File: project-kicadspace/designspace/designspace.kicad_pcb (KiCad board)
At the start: 2 copper layers, 39 parts, among them J1 PJ-313B, U3 MAX9812

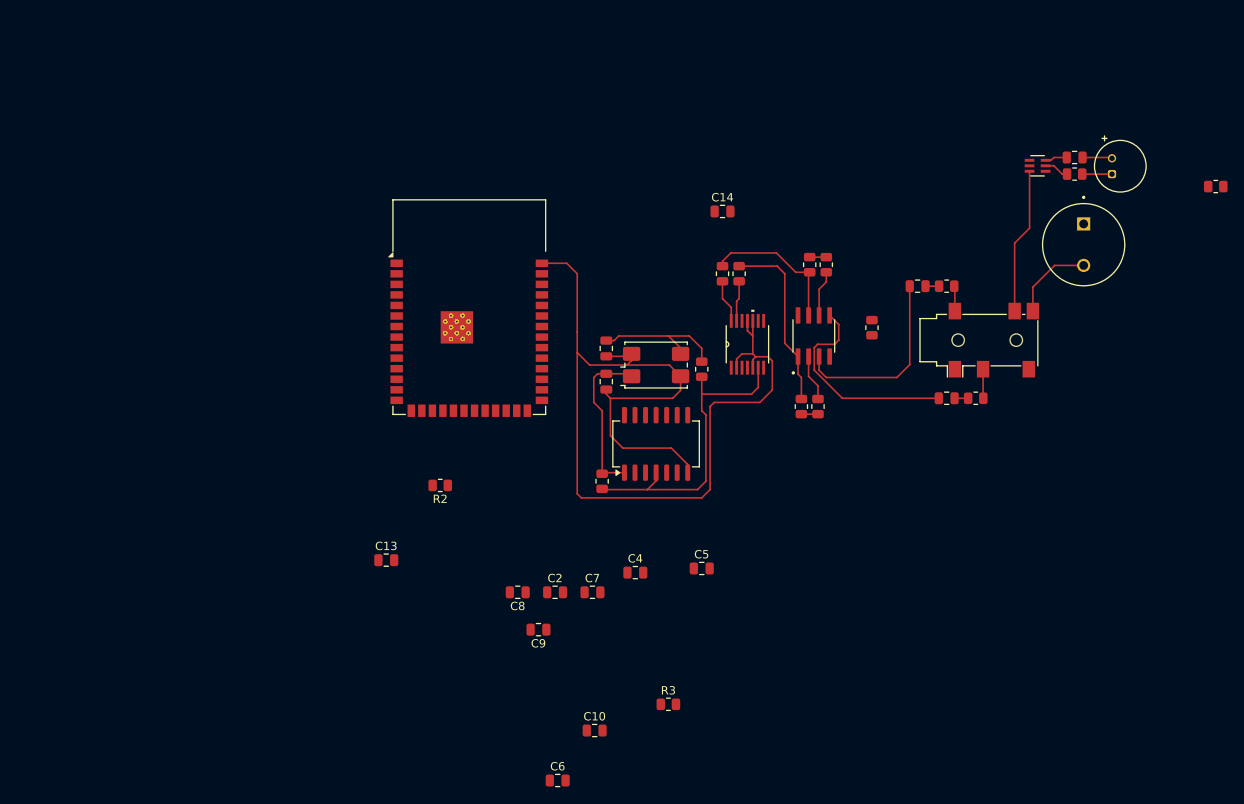
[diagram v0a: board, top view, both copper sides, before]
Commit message: feat(pcb): add kit footprint for esp32 & inital placing
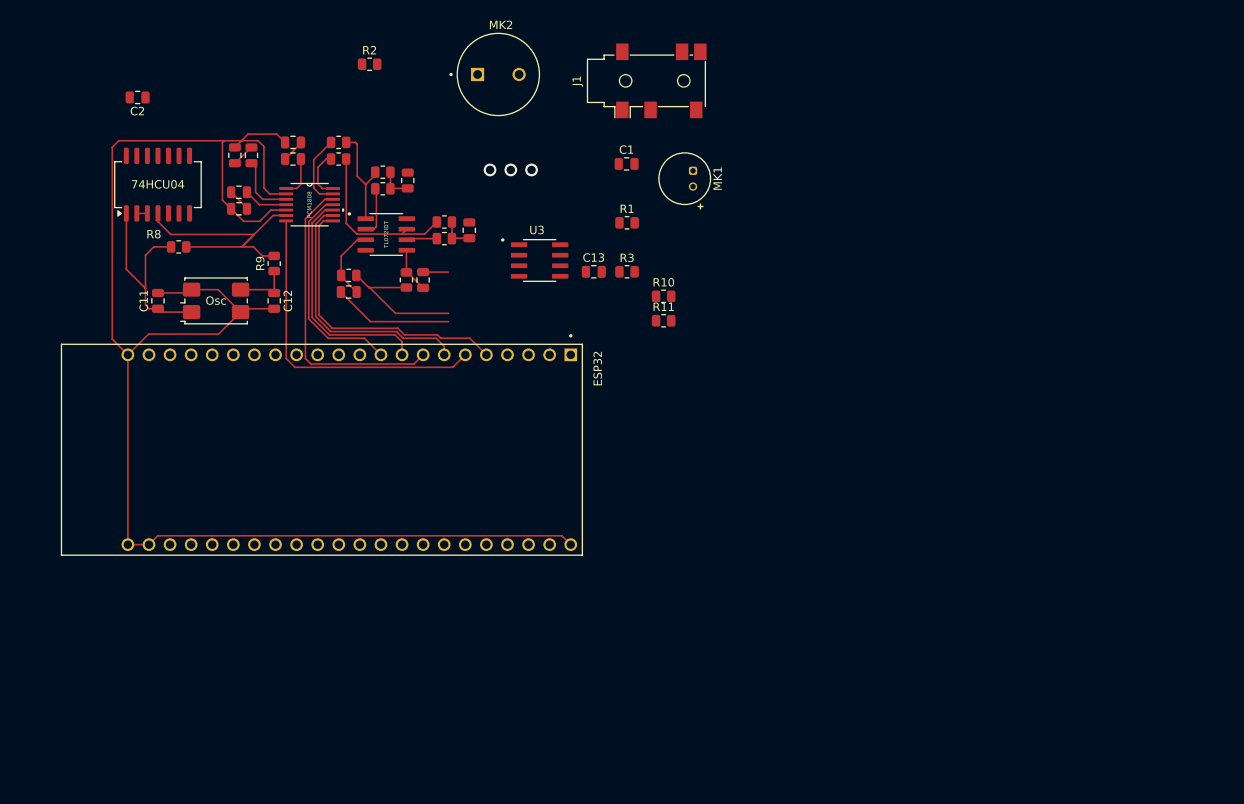
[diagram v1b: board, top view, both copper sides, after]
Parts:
- removed INVBUF1: 74HCU04, Package_SO:SO-14_5.3x10.2mm_P1.27mm
- removed Op-amp2: TL072, tl072:TL072IDT
- removed Osc1: 24.576MHz, Crystal:Crystal_SMD_7050-4Pin_7.0x5.0mm
- added 74HCU04: 74HCU04, Package_SO:SO-14_5.3x10.2mm_P1.27mm, F.Cu at (59.0, 70.3)
- added Osc: 24.576MHz, Crystal:Crystal_SMD_7050-4Pin_7.0x5.0mm, F.Cu at (66.0, 84.3)
- added TL072IDT: TL072, tl072:TL072IDT, F.Cu at (86.5, 76.3)
- ESP32: value ESP32-S3-WROOM-1 -> ESP32-S3-DEVKITC-1-N8R8; footprint RF_Module:ESP32-S3-WROOM-1 -> esp32-s3-kit:ESP32-S3-DEVKITC-1-N8R8
- U3: footprint max9812:MAX9812 -> tl072:TL072IDT
- moved R7 105.0 mm to (82.0, 81.2), turned to 180 degrees
- moved C6 83.2 mm to (75.3, 65.2), turned to 180 degrees
- moved C2 78.0 mm to (56.5, 59.8), turned to 180 degrees
- moved C5 75.1 mm to (68.3, 66.7), turned to -90 degrees
- moved MK2 73.4 mm to (100.0, 57.0), turned to 0 degrees
- moved C10 70.0 mm to (89.1, 69.8), turned to -90 degrees
- moved C3 68.5 mm to (82.0, 83.2), turned to 180 degrees
- moved C4 68.3 mm to (70.3, 66.7), turned to 90 degrees
- moved C15 64.7 mm to (90.9, 81.8), turned to 90 degrees
- moved C7 63.4 mm to (75.3, 67.2)
- moved C9 62.2 mm to (68.8, 73.2), turned to 0 degrees
- moved U3 61.0 mm to (105.0, 79.4)
- moved C8 58.7 mm to (68.8, 71.2)
- moved R5 58.6 mm to (86.1, 70.8), turned to 0 degrees
- moved R8 58.3 mm to (61.5, 77.8), turned to 0 degrees
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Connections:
- C6 pad 1: Net-(PCM1808-VREF) -> Net-(C6-Pad1)
- C6 pad 2: Net-(C6-Pad2) -> GND
- C7 pad 1: GND -> Net-(C6-Pad1)
- C7 pad 2: Net-(C6-Pad2) -> Net-(PCM1808-VREF)
- PCM1808 pad 10: GND -> Net-(PCM1808-MD0)
- PCM1808 pad 11: GND -> Net-(PCM1808-MD1)
- PCM1808 pad 12: Net-(ESP32-IO3) -> Net-(PCM1808-FMT)
- PCM1808 pad 7: Net-(ESP32-IO6) -> Net-(PCM1808-LRCK)
- PCM1808 pad 8: Net-(ESP32-IO5) -> Net-(PCM1808-BCK)
- PCM1808 pad 9: Net-(ESP32-IO7) -> Net-(PCM1808-DOUT)
- R12 pad 2: Net-(Op-amp2A-+) -> Net-(C13-Pad2)
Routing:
- net GND: track 133.4 -> 184.5 mm
- net Net-(PCM1808-LRCK): track 0.00 -> 39.2 mm
- net Net-(PCM1808-FMT): track 0.00 -> 36.0 mm
- net Net-(PCM1808-BCK): track 0.00 -> 34.8 mm
- net Net-(PCM1808-DOUT): track 0.00 -> 31.6 mm
- net Net-(PCM1808-MD0): track 0.00 -> 28.1 mm
- net Net-(PCM1808-MD1): track 0.00 -> 26.0 mm
- net Net-(Op-amp2B-+): track 25.9 -> 5.45 mm
- net Net-(U3-OUT): track 17.6 -> 0.00 mm
- net Net-(C13-Pad2): track 0.00 -> 17.4 mm
- net Net-(Op-amp2A-+): track 23.0 -> 8.87 mm
- net Net-(C3-Pad2): track 1.64 -> 14.4 mm
- net Net-(MK2-+): track 10.1 -> 0.00 mm
- net Net-(C12-Pad1): track 16.7 -> 6.85 mm
- net Net-(Op-amp2-Pad1): track 21.8 -> 12.8 mm
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
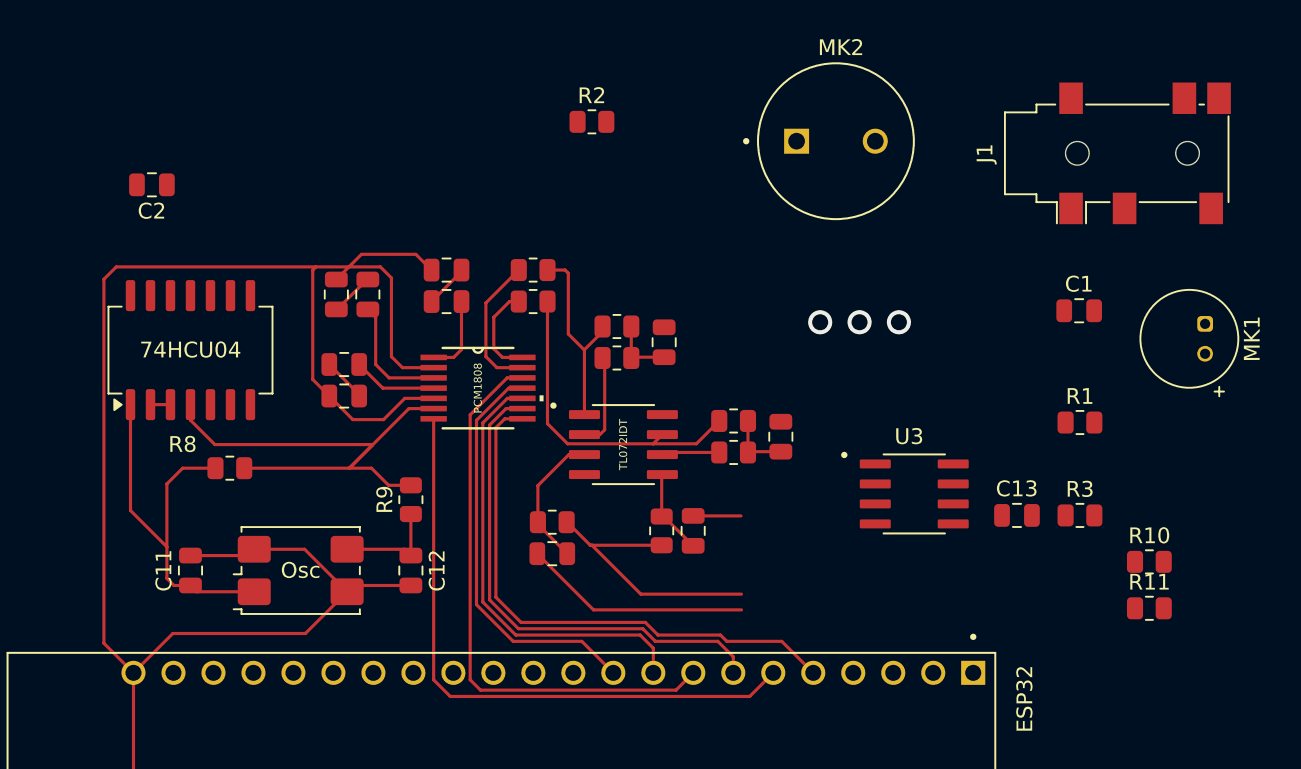
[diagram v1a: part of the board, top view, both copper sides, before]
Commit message: feat(pcb): add routing to pj342s, max9812, tct4016r
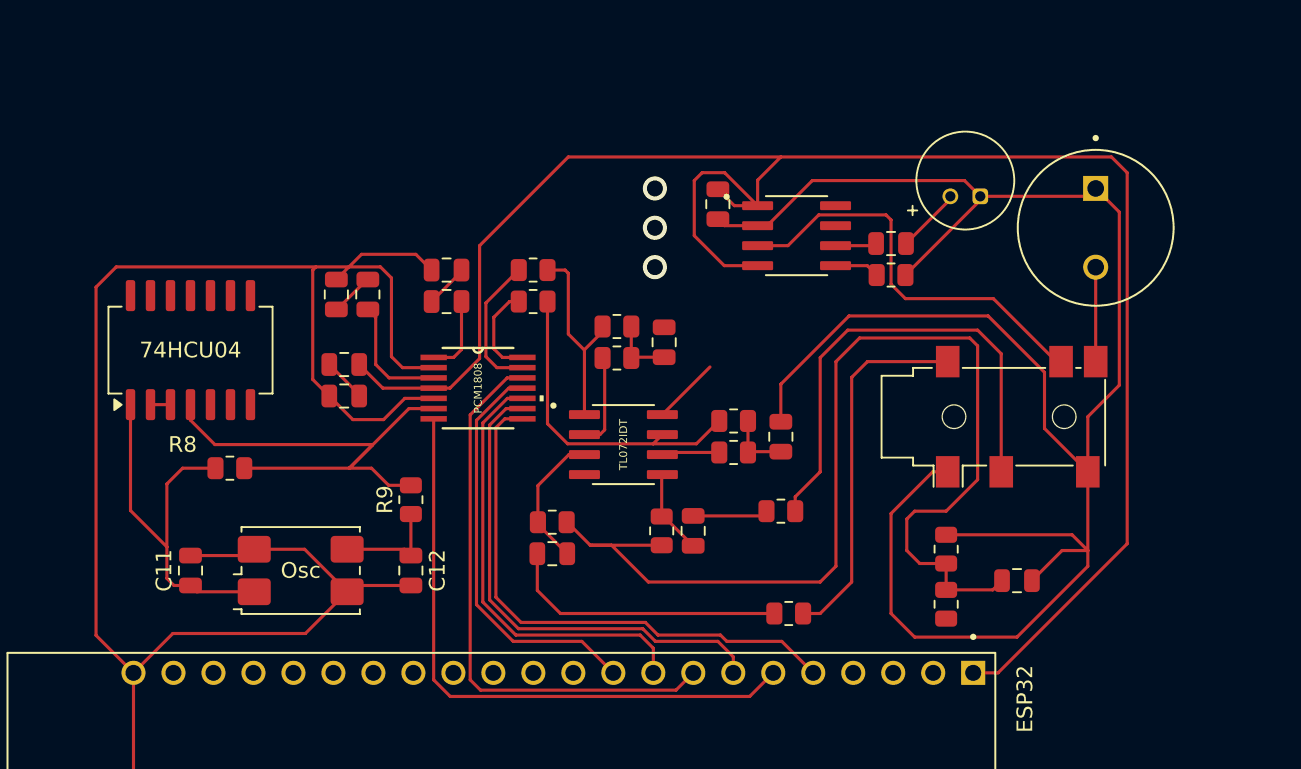
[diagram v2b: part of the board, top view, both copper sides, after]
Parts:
- J1: value PJ-313B -> PJ-342S
- moved R2 38.0 mm to (107.0, 86.4), turned to 90 degrees
- moved C2 36.0 mm to (92.5, 61.0), turned to -90 degrees
- moved R11 24.2 mm to (96.5, 80.5)
- moved R10 23.1 mm to (97.0, 87.0)
- moved J1 18.5 mm to (111.8, 74.5)
- moved U3 18.0 mm to (97.5, 63.0)
- moved MK2 17.4 mm to (116.5, 62.5), turned to -90 degrees
- moved MK1 16.4 mm to (109.2, 60.5), turned to 180 degrees
- moved R1 15.2 mm to (103.5, 65.5)
- moved C1 12.7 mm to (103.5, 63.5)
- moved R3 8.77 mm to (107.0, 82.9), turned to 90 degrees
- moved C13 4.14 mm to (111.5, 84.9), turned to 180 degrees
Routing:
- net GND: track 184.5 -> 313.0 mm
- net 3.3V: track 5.35 -> 116.9 mm
- net Net-(C13-Pad2): track 17.4 -> 70.7 mm
- net Net-(J1-PadR1): track 0.00 -> 30.8 mm
- net Net-(U3-OUT): track 0.00 -> 26.3 mm
- net Net-(J1-PadT): track 0.00 -> 23.4 mm
- net Net-(MK2-+): track 0.00 -> 6.00 mm
- net 9V: track 0.00 -> 4.28 mm
- net Net-(MK1-+): track 0.00 -> 4.17 mm
- net Net-(C3-Pad2): track 14.4 -> 18.0 mm
- net Net-(U3-BIAS): track 0.00 -> 2.86 mm
- net Net-(U3-IN): track 0.00 -> 2.63 mm
- net Net-(C15-Pad2): track 3.04 -> 4.78 mm

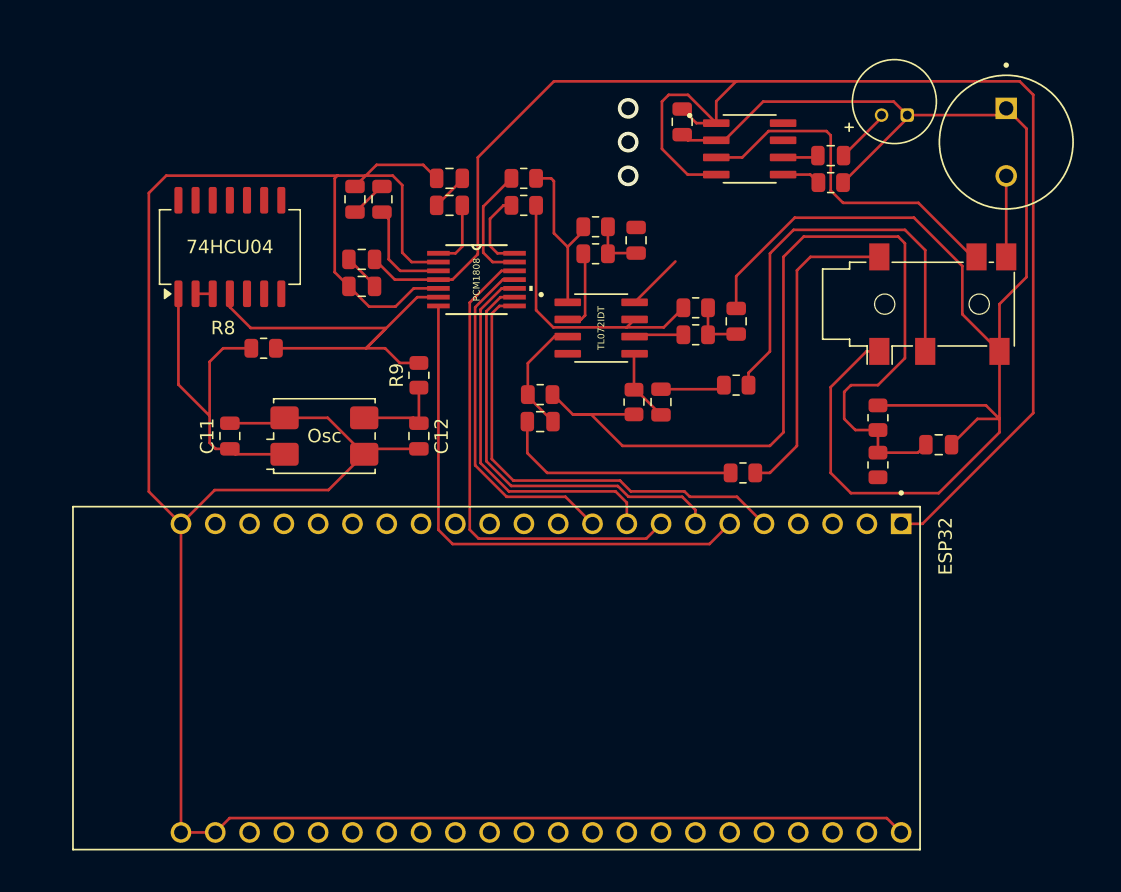
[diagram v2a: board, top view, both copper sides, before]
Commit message: feat(pcb): add ground planning to hide ground tracks
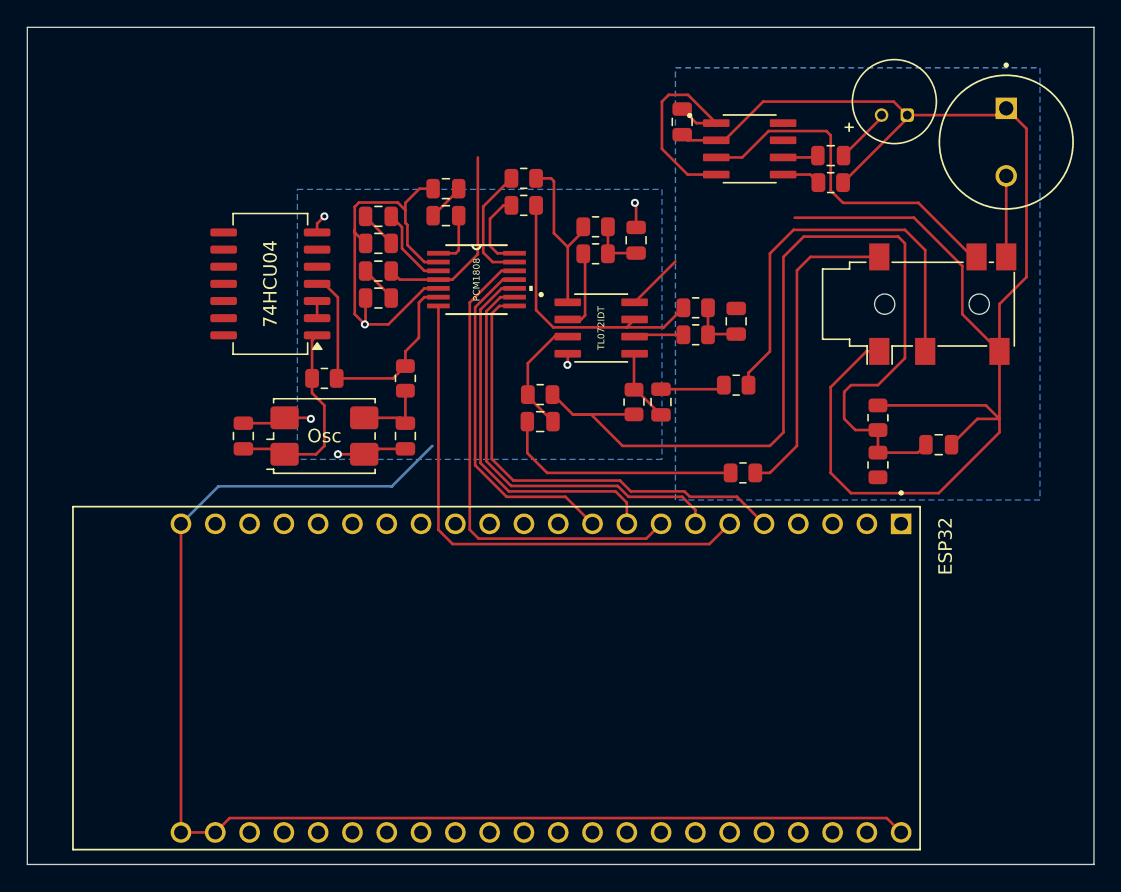
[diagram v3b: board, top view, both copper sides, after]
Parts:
- moved R8 5.02 mm to (66.0, 80.0)
- moved 74HCU04 4.06 mm to (62.0, 73.0), turned to 180 degrees
- moved C5 3.70 mm to (70.0, 70.0), turned to 0 degrees
- moved C8 1.51 mm to (70.0, 72.0)
- moved C9 1.51 mm to (70.0, 74.0)
- moved C4 1.29 mm to (70.0, 68.0), turned to 180 degrees
- moved R9 1.03 mm to (72.0, 80.0)
- moved C11 1.00 mm to (60.0, 84.3)
- moved C12 1.00 mm to (72.0, 84.3)
- moved C6 0.81 mm to (75.0, 66.0)
- moved C7 0.81 mm to (75.0, 68.0)
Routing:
- net 3.3V: track 116.9 -> 31.0 mm
- net GND: track 313.0 -> 263.6 mm, vias 0 -> 6
- net Net-(PCM1808-SCKI): track 33.2 -> 20.2 mm
- net Net-(C11-Pad1): track 25.4 -> 15.1 mm
- net 5V: track 7.74 -> 6.09 mm
- net Net-(C12-Pad1): track 6.85 -> 5.62 mm
- net Net-(PCM1808-VREF): track 5.03 -> 4.16 mm
- net (no net): vias 3 -> 0
- added copper zone on B.Cu, net GND
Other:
- board outline added: 79 x 62 mm
- board text added: "C9"

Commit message: feat(pcb): add 3 hole pin for MAX9812 complete board
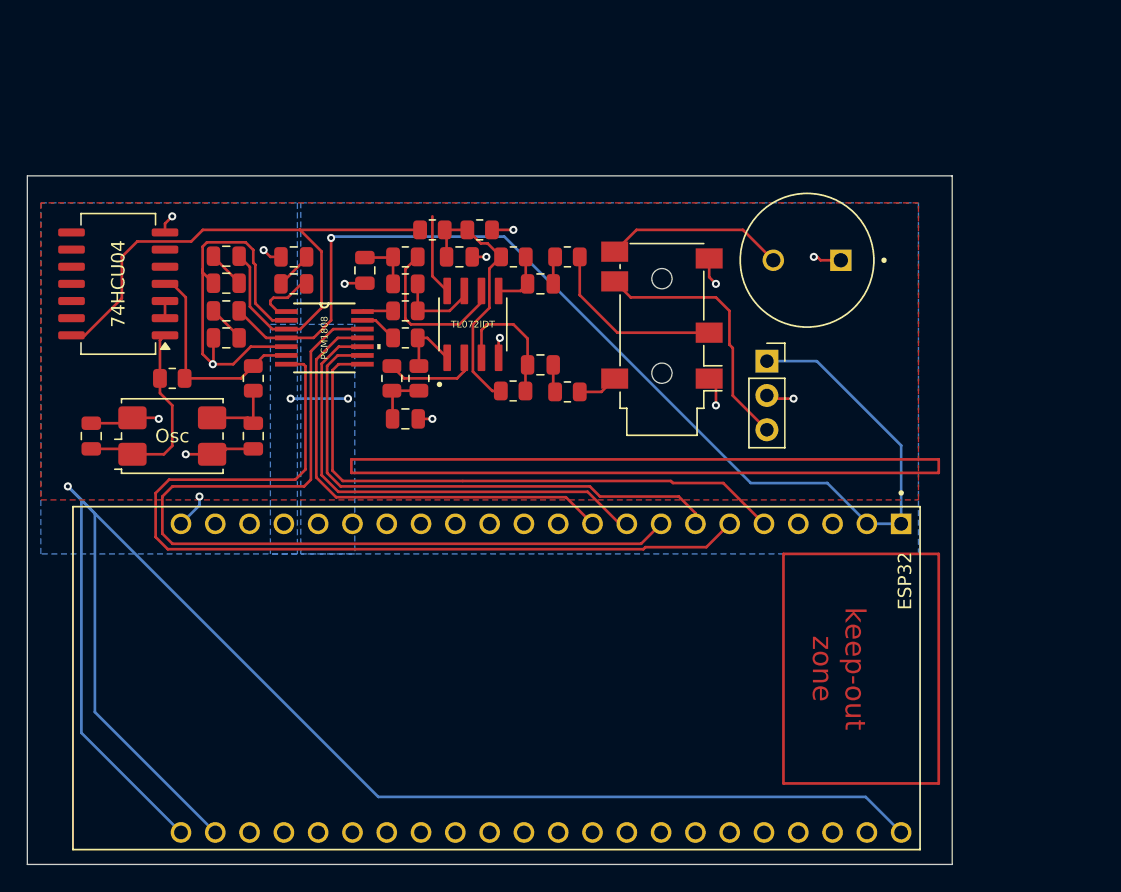
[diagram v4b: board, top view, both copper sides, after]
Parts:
- removed C1, C2: 0.1uF, Capacitor_SMD:C_0805_2012Metric
- removed MK1: Microphone, Sensor_Audio:POM-2244P-C3310-2-R
- removed R1: 2.2kOhm, Resistor_SMD:R_0805_2012Metric
- removed U3: MAX9812, tl072:TL072IDT
- added REF**: PinSocket_1x03_P2.54mm_Vertical, Connector_PinSocket_2.54mm:PinSocket_1x03_P2.54mm_Vertical, F.Cu at (98.8, 78.7)
- moved C13 38.1 mm to (76.0, 71.0)
- moved R2 37.3 mm to (74.0, 69.0), turned to 0 degrees
- moved R3 32.6 mm to (77.5, 69.0), turned to 0 degrees
- moved C14 27.8 mm to (69.0, 72.0), turned to 90 degrees
- moved R14 22.3 mm to (72.0, 71.0), turned to 180 degrees
- moved C10 21.6 mm to (72.0, 83.0), turned to 180 degrees
- moved R13 21.6 mm to (72.0, 73.0), turned to 180 degrees
- moved J1 20.8 mm to (91.0, 75.3), turned to 180 degrees
- moved R5 17.7 mm to (71.0, 80.0), turned to -90 degrees
- moved R4 17.2 mm to (73.0, 80.0), turned to -90 degrees
- moved MK2 17.2 mm to (101.8, 71.2), turned to 180 degrees
- moved R11 15.7 mm to (84.0, 71.0)
- moved R6 14.7 mm to (72.0, 77.0)
- moved R10 14.3 mm to (84.0, 81.0)
- moved R12 14.0 mm to (80.0, 71.0), turned to 180 degrees
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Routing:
- net GND: track 263.6 -> 196.1 mm, vias 6 -> 18
- net 3.3V: track 31.0 -> 83.7 mm, vias 0 -> 1
- net Net-(C13-Pad2): track 70.7 -> 19.1 mm
- net 5V: track 6.09 -> 48.0 mm
- net Net-(PCM1808-FMT): track 36.0 -> 66.1 mm
- net Net-(PCM1808-LRCK): track 39.2 -> 67.9 mm
- net Net-(J1-PadT): track 23.4 -> 3.00 mm
- net Net-(J1-PadR1): track 30.8 -> 13.6 mm
- net Net-(C3-Pad2): track 18.0 -> 2.06 mm
- net Net-(Op-amp2-Pad7): track 20.6 -> 6.29 mm
- net Net-(PCM1808-MD1): track 26.0 -> 34.7 mm
- net Net-(Op-amp2B--): track 3.67 -> 12.3 mm
- net Net-(PCM1808-BCK): track 34.8 -> 43.4 mm
- net Net-(PCM1808-DOUT): track 31.6 -> 40.2 mm
- net Net-(Op-amp2-Pad1): track 12.8 -> 4.92 mm
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- added copper zone on F.Cu, net GND
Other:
- board size 79 x 62 mm -> 68.5 x 51 mm
- board text added: "keep-out zone"
